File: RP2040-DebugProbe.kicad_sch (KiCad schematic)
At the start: 34 parts, among them J10 CONN_USB, J7 CONN_JTAG, SW1 BOOTSEL, U1 W25Q128JVS, U2 RP2040, U4 W25Q128JVEIQ, U5 AMS1117-3.3, Y1 12MHz

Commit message: Improved schematics
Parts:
- added C12, C13, C17: 100nF, Capacitor_SMD:C_0402_1005Metric, symbol Device:C_Small
- added D1, D6: GREEN, LED_SMD:LED_0603_1608Metric, symbol Device:LED_Small
- added D4, D7: YELLOW, LED_SMD:LED_0603_1608Metric, symbol Device:LED_Small
- added D5: RED, LED_SMD:LED_0603_1608Metric, symbol Device:LED_Small
- added J1: CONN_MCU_JTAG, Connector_PinHeader_1.27mm:PinHeader_2x05_P1.27mm_Vertical, symbol Connector:Conn_ARM_JTAG_SWD_10
- added J2: CONN_MCU_UART, Connector_PinHeader_2.54mm:PinHeader_1x03_P2.54mm_Vertical, symbol Connector_Generic:Conn_01x03
- added J3: CONN_DBG_COMB, symbol Connector_Generic:Conn_01x08
- added J4: CONN_3V3_JUMPER, Connector_PinSocket_2.54mm:PinSocket_1x02_P2.54mm_Vertical, symbol Connector_Generic:Conn_01x02
- added R1, R2, R3, R4, R5: 1k, Resistor_SMD:R_0402_1005Metric, symbol Device:R_Small
- added R13, R14, R15, R16, R17, R9: 100R, Resistor_SMD:R_0402_1005Metric, symbol Device:R_Small
- added R8: 10k, Resistor_SMD:R_0402_1005Metric, symbol Device:R_Small
- added U3, U6: 74AUP1T17, SN74AUP1T17DCKR:SOT65P210X110-5N, symbol SN74AUP1T17DCKR:SN74AUP1T17DCKR
- J7: value CONN_JTAG -> CONN_DBG_JTAG
- R6: value 5k1 -> 1k
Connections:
- net VUSB is gone; now on net +5V: FB2.2
- net +3V3: now also C13.1, C17.1, J1.1 (VTref), J3.5 (Pin_5), J4.1 (Pin_1), R8.2, U3.5 (VCC), U6.5 (VCC); no longer J7.1 (VTref)
- net +5V: now also J3.4 (Pin_4); no longer D3.4 (VCC), FB2.1, J10.A4 (VBUS), J10.A9 (VBUS), J10.B4 (VBUS), J10.B9 (VBUS)
- net GND: now also C12.2, C13.2, C17.2, D1.1 (K), D4.1 (K), D5.1 (K), D6.1 (K), D7.1 (K), J1.3 (GND), J1.5 (GND), J1.9 (GNDDetect), J2.2 (Pin_2), J3.2 (Pin_2), J3.7 (Pin_7), U3.3 (GND), U6.3 (GND)
- net LED_TX: now reaches U2.11 (GPIO8)
- net LED_TX: now also R2.1
- net DBG_DIO: now reaches U2.17 (GPIO14)
- net DBG_DIO: now also R16.2
- net LED_ACT: now reaches U2.4 (GPIO2)
- net LED_ACT: now also R3.1
- net D0_RX renamed MCU_RX
- net MCU_RX: now also J2.3 (Pin_3)
- net D10_SS renamed UART_RX_BUF
- net UART_RX_BUF: now also U3.4 (Y)
- net D11_MOSI renamed LED_RX
- net LED_RX: now also R1.1
- net D12_MISO renamed UART_TX
- net UART_TX: now also R15.2
- net D13_SCK renamed UART_RX
- net UART_RX: now also R14.2
- net D14_A0: no longer names the net of U2.38 (GPIO26_ADC0)
- net D15_A1: no longer names the net of U2.39 (GPIO27_ADC1)
- net D16_A2: no longer names the net of U2.40 (GPIO28_ADC2)
- net D17_A3: no longer names the net of U2.41 (GPIO29_ADC3)
- net D18_SDA renamed DBG_CLK
- net DBG_CLK: now also R17.2
- net D19_SCL renamed DBG_DIO_BUF
- net DBG_DIO_BUF: now also U6.4 (Y)
- net D1_TX renamed MCU_TX
- net MCU_TX: now also J2.1 (Pin_1)
- net D2: no longer names the net of U2.37 (GPIO25)
- net D20: no longer names the net of U2.34 (GPIO22)
- net D21: no longer names the net of U2.35 (GPIO23)
- net D3 renamed LED_CON
- net LED_CON: now also R4.1
- net D4 renamed LED_RUN
- net LED_RUN: now also R5.1
- net D5: no longer names the net of U2.28 (GPIO17)
- net D6: no longer names the net of U2.29 (GPIO18)
- net D7: no longer names the net of U2.30 (GPIO19)
- net D8: no longer names the net of U2.31 (GPIO20)
- net D9: no longer names the net of U2.32 (GPIO21)
- net LED_B: no longer names the net of U2.14 (GPIO11)
- net LED_G: no longer names the net of U2.13 (GPIO10)
- net LED_R: no longer names the net of U2.12 (GPIO9)
- net RESET: no longer names the net of J7.10 (~{RESET})
- net RESET: no longer U2.26 (RUN)
- net SWCLK renamed MCU_CLK
- net MCU_CLK: now also J1.4 (SWDCLK/TCK); no longer J7.4 (SWDCLK/TCK)
- net SWD renamed MCU_DIO
- net MCU_DIO: now also J1.2 (SWDIO/TMS); no longer J7.2 (SWDIO/TMS)
- new net: R13.2, U6.2 (A)
- new net: D1.2 (A), R1.2
- new net: R9.2, U3.2 (A)
- new net: D5.2 (A), R3.2
- new net: D6.2 (A), R4.2
- new net: D4.2 (A), R2.2
- new net: D7.2 (A), R5.2
- new net MCU_RESET: C12.1, J1.10 (~{RESET}), R8.1, U2.26 (RUN)
- new net TARGET_3V3: J4.2 (Pin_2), J7.1 (VTref)
- new net TARGET_CLK: J3.6 (Pin_6), J7.4 (SWDCLK/TCK), R17.1
- new net TARGET_DIO: J3.8 (Pin_8), J7.2 (SWDIO/TMS), R13.1, R16.1
- new net TARGET_RX: J3.3 (Pin_3), R14.1, R9.1
- new net TARGET_TX: J3.1 (Pin_1), R15.1
- new net VBUS: D3.4 (VCC), FB2.1, J10.A4 (VBUS), J10.A9 (VBUS), J10.B4 (VBUS), J10.B9 (VBUS)
- no-connect marks 9 -> 24
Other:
- note added: "MCU JTAG connector"
- note added: "MCU Reset line"
- note added: "MCU UART connector"
- note added: "Status indication LEDs"
- note added: "Target JTAG connector"
- note added: "Target protection"
- note removed: "JATG connector"
- moved on the sheet: C14, C15, C19, C20, C21, D2, D3, J7, R12, R6, U5, Y1

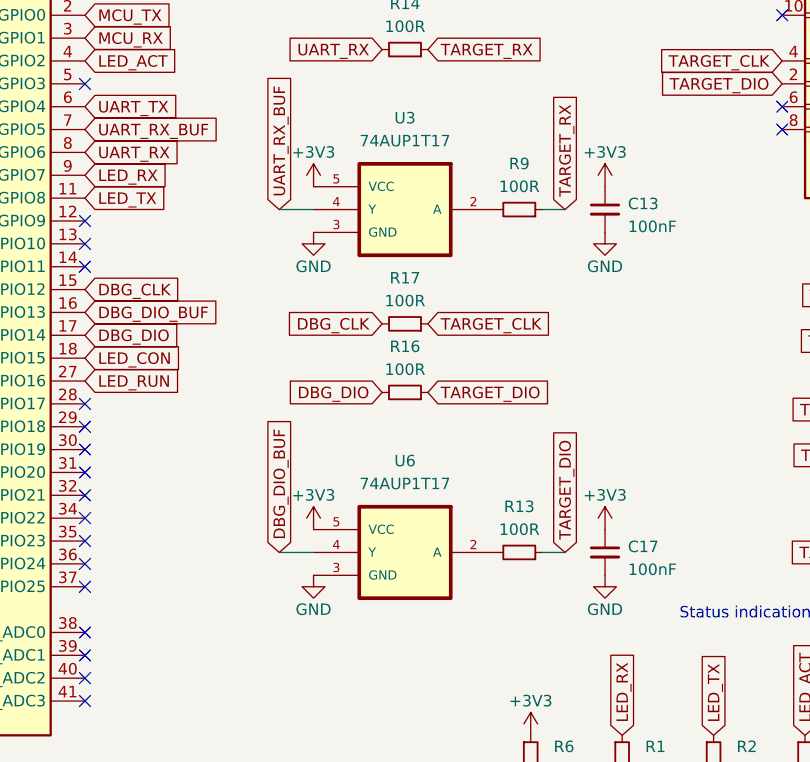
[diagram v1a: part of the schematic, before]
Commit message: Added basic board layout
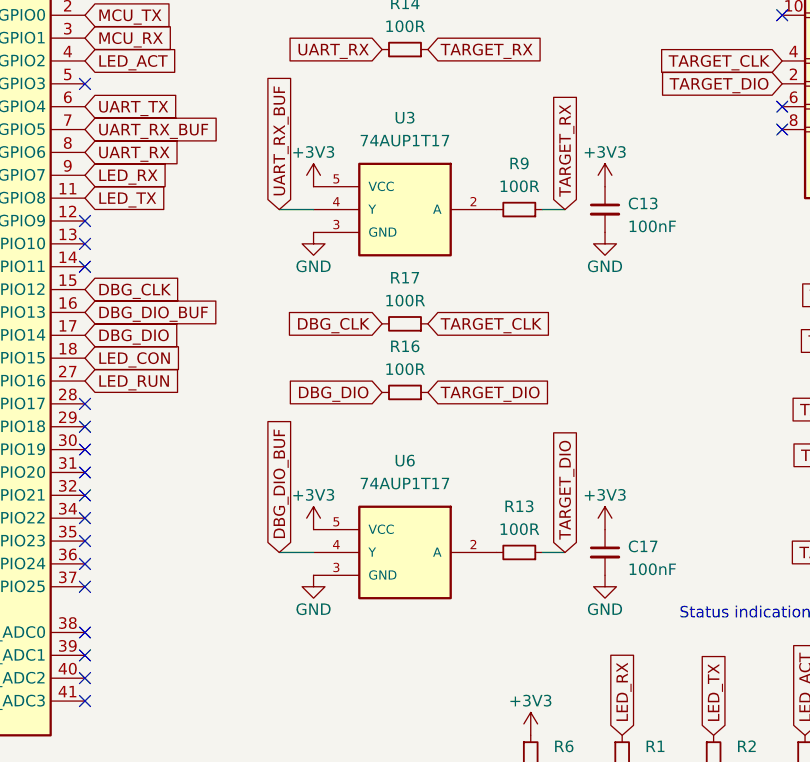
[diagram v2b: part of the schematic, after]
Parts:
- J3: footprint (none) -> Connector_PinSocket_2.54mm:PinSocket_1x08_P2.54mm_Vertical
- U3, U6: footprint SN74AUP1T17DCKR:SOT65P210X110-5N -> Package_TO_SOT_SMD:SOT-353_SC-70-5
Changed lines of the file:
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@@
       (effects (font (size 1.27 1.27)) (justify left))
     )
-    (property "Footprint" "" (at 263.525 76.835 0)
+    (property "Footprint" "Connector_PinSocket_2.54mm:PinSocket_1x08_P2.54mm_Vertical" (at 263.525 76.835 0)
       (effects (font (size 1.27 1.27)) hide)
     )
@@
       (effects (font (size 1.27 1.27)))
     )
-    (property "Footprint" "SN74AUP1T17DCKR:SOT65P210X110-5N" (at 287.02 99.06 0)
+    (property "Footprint" "Package_TO_SOT_SMD:SOT-353_SC-70-5" (at 287.02 99.06 0)
       (effects (font (size 1.27 1.27)) (justify bottom) hide)
     )
@@
     )
   )
-  (symbol (lib_id "SN74AUP1T17DCKR:SN74AUP1T17DCKR") (at 201.93 62.23 0) (mirror y) (unit 1)
+  (symbol (lib_name "SN74AUP1T17DCKR_1") (lib_id "SN74AUP1T17DCKR:SN74AUP1T17DCKR") (at 201.93 62.23 0) (mirror y) (unit 1)
     (in_bom yes) (on_board yes) (dnp no) (fields_autoplaced)
     (property "Reference" "U3" (at 201.93 49.53 0)
@@
       (effects (font (size 1.27 1.27)))
     )
-    (property "Footprint" "SN74AUP1T17DCKR:SOT65P210X110-5N" (at 287.02 60.96 0)
-      (effects (font (size 1.27 1.27)) (justify bottom) hide)
-    )
+    (property "Footprint" "Package_TO_SOT_SMD:SOT-353_SC-70-5" (at 287.02 60.96 0)
+      (effects (font (size 1.27 1.27)) (justify bottom) hide)
+    )

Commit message: Placed components on their approximate locations. Added board approximate outline.
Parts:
- removed C22: 100nF, Capacitor_SMD:C_0402_1005Metric, symbol Device:C_Small
- J3: footprint Connector_PinSocket_2.54mm:PinSocket_1x08_P2.54mm_Vertical -> Connector_PinHeader_2.54mm:PinHeader_1x08_P2.54mm_Vertical
- J4: footprint Connector_PinSocket_2.54mm:PinSocket_1x02_P2.54mm_Vertical -> Connector_PinHeader_2.54mm:PinHeader_1x02_P2.54mm_Vertical
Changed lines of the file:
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@@
       (effects (font (size 1.27 1.27)) (justify left))
     )
-    (property "Footprint" "Connector_PinSocket_2.54mm:PinSocket_1x08_P2.54mm_Vertical" (at 263.525 76.835 0)
+    (property "Footprint" "Connector_PinHeader_2.54mm:PinHeader_1x08_P2.54mm_Vertical" (at 263.525 76.835 0)
       (effects (font (size 1.27 1.27)) hide)
     )
@@
         (path "/9a38a81c-7302-494f-9784-2ab4342a0a1d"
           (reference "#PWR067") (unit 1)
-        )
-      )
-    )
-  )
-  (symbol (lib_id "Device:C_Small") (at 273.05 151.13 0) (unit 1)
-    (in_bom yes) (on_board yes) (dnp no) (fields_autoplaced)
-    (property "Reference" "C22" (at 275.59 150.5013 0)
-      (effects (font (size 1.27 1.27)) (justify left))
-    )
-    (property "Value" "100nF" (at 275.59 153.0413 0)
-      (effects (font (size 1.27 1.27)) (justify left))
-    )
-    (property "Footprint" "Capacitor_SMD:C_0402_1005Metric" (at 273.05 151.13 0)
-      (effects (font (size 1.27 1.27)) hide)
-    )
-    (property "Datasheet" "~" (at 273.05 151.13 0)
-      (effects (font (size 1.27 1.27)) hide)
-    )
-    (pin "1")
-    (pin "2")
-    (instances
-      (project "RP2040-DebugProbe"
-        (path "/9a38a81c-7302-494f-9784-2ab4342a0a1d"
-          (reference "C22") (unit 1)
         )
       )
@@
       (effects (font (size 1.27 1.27)) (justify left))
     )
-    (property "Footprint" "Connector_PinSocket_2.54mm:PinSocket_1x02_P2.54mm_Vertical" (at 263.525 95.25 0)
+    (property "Footprint" "Connector_PinHeader_2.54mm:PinHeader_1x02_P2.54mm_Vertical" (at 263.525 95.25 0)
       (effects (font (size 1.27 1.27)) hide)
     )
@@
     )
   )
-  (symbol (lib_id "power:GND") (at 273.05 153.67 0) (unit 1)
-    (in_bom yes) (on_board yes) (dnp no)
-    (property "Reference" "#PWR077" (at 273.05 160.02 0)
-      (effects (font (size 1.27 1.27)) hide)
-    )
-    (property "Value" "GND" (at 273.05 157.48 0)
-      (effects (font (size 1.27 1.27)))
-    )
-    (property "Footprint" "" (at 273.05 153.67 0)
-      (effects (font (size 1.27 1.27)) hide)
-    )
-    (property "Datasheet" "" (at 273.05 153.67 0)
-      (effects (font (size 1.27 1.27)) hide)
-    )
-    (pin "1")
-    (instances
-      (project "RP2040-DebugProbe"
-        (path "/9a38a81c-7302-494f-9784-2ab4342a0a1d"
-          (reference "#PWR077") (unit 1)
-        )
-      )
-    )
-  )
   (symbol (lib_id "Device:C_Small") (at 92.71 93.98 0) (unit 1)
     (in_bom yes) (on_board yes) (dnp no) (fields_autoplaced)
@@
         )
       )
-    )
-  )
-  (symbol (lib_id "power:+1V1") (at 273.05 148.59 0) (unit 1)
-    (in_bom yes) (on_board yes) (dnp no) (fields_autoplaced)
-    (property "Reference" "#PWR076" (at 273.05 152.4 0)
-      (effects (font (size 1.27 1.27)) hide)
-    )
-    (property "Value" "+1V1" (at 273.05 144.78 0)
-      (effects (font (size 1.27 1.27)))
-    )
-    (property "Footprint" "" (at 273.05 148.59 0)
-      (effects (font (size 1.27 1.27)) hide)
-    )
-    (property "Datasheet" "" (at 273.05 148.59 0)
-      (effects (font (size 1.27 1.27)) hide)
-    )
-    (pin "1")
-    (instances
-      (project "RP2040-DebugProbe"
-        (path "/9a38a81c-7302-494f-9784-2ab4342a0a1d"
-          (reference "#PWR076") (unit 1)
-        )
-      )

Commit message: Moved stuff around
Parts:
- added C18: 100nF, Capacitor_SMD:C_0402_1005Metric, symbol Device:C_Small
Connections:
- net +1V1: now also C18.1
- net GND: now also C18.2
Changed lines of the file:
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@@
+    )
+  )
+  (symbol (lib_id "power:+1V1") (at 272.415 148.59 0) (unit 1)
+    (in_bom yes) (on_board yes) (dnp no) (fields_autoplaced)
+    (property "Reference" "#PWR072" (at 272.415 152.4 0)
+      (effects (font (size 1.27 1.27)) hide)
+    )
+    (property "Value" "+1V1" (at 272.415 144.78 0)
+      (effects (font (size 1.27 1.27)))
+    )
+    (property "Footprint" "" (at 272.415 148.59 0)
+      (effects (font (size 1.27 1.27)) hide)
+    )
+    (property "Datasheet" "" (at 272.415 148.59 0)
+      (effects (font (size 1.27 1.27)) hide)
+    )
+    (pin "1")
+    (instances
+      (project "RP2040-DebugProbe"
+        (path "/9a38a81c-7302-494f-9784-2ab4342a0a1d"
+          (reference "#PWR072") (unit 1)
+        )
+      )
     )
   )
@@
         (path "/9a38a81c-7302-494f-9784-2ab4342a0a1d"
           (reference "#PWR071") (unit 1)
+        )
+      )
+    )
+  )
+  (symbol (lib_id "power:GND") (at 272.415 153.67 0) (unit 1)
+    (in_bom yes) (on_board yes) (dnp no)
+    (property "Reference" "#PWR073" (at 272.415 160.02 0)
+      (effects (font (size 1.27 1.27)) hide)
+    )
+    (property "Value" "GND" (at 272.415 157.48 0)
+      (effects (font (size 1.27 1.27)))
+    )
+    (property "Footprint" "" (at 272.415 153.67 0)
+      (effects (font (size 1.27 1.27)) hide)
+    )
+    (property "Datasheet" "" (at 272.415 153.67 0)
+      (effects (font (size 1.27 1.27)) hide)
+    )
+    (pin "1")
+    (instances
+      (project "RP2040-DebugProbe"
+        (path "/9a38a81c-7302-494f-9784-2ab4342a0a1d"
+          (reference "#PWR073") (unit 1)
         )
       )
@@
         )
       )
+    )
+  )
+  (symbol (lib_id "Device:C_Small") (at 272.415 151.13 0) (unit 1)
+    (in_bom yes) (on_board yes) (dnp no) (fields_autoplaced)
+    (property "Reference" "C18" (at 274.955 150.5013 0)
+      (effects (font (size 1.27 1.27)) (justify left))
+    )
+    (property "Value" "100nF" (at 274.955 153.0413 0)
+      (effects (font (size 1.27 1.27)) (justify left))
+    )
+    (property "Footprint" "Capacitor_SMD:C_0402_1005Metric" (at 272.415 151.13 0)
+      (effects (font (size 1.27 1.27)) hide)
+    )
+    (property "Datasheet" "~" (at 272.415 151.13 0)
+      (effects (font (size 1.27 1.27)) hide)
+    )
+    (pin "1")
+    (pin "2")
+    (instances
+      (project "RP2040-DebugProbe"
+        (path "/9a38a81c-7302-494f-9784-2ab4342a0a1d"
+          (reference "C18") (unit 1)
+        )
+      )
